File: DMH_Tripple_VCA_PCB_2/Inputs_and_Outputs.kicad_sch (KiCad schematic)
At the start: 0 parts

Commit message: Corrected header locations and placed pcb2 comps
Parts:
- added D6, D7, D8: LED_Dual_AKA, SynthStuff:LED_D3.0mm-2color, symbol Device:LED_Dual_AKA
- added J0: Conn_01x01, Connector_PinHeader_2.54mm:PinHeader_1x01_P2.54mm_Vertical, symbol Connector_Generic:Conn_01x01
- added J1, J10, J2, J3, J4, J5, J6, J7, J8, J9: TS_Jack_6.35mm_Sw, SynthStuff:CUI_MJ-63052A, symbol SynthStuff:TS_Jack_6.35mm_Sw
- added J200: IDC_02x05, SynthStuff:IDC-Header_2x05_P2.54mm_Vertical_BackBone, symbol SynthStuff:BackBone_Connector_10Pin
- added J50, J60, J70: Conn_01x06, Connector_PinHeader_2.54mm:PinHeader_1x06_P2.54mm_Vertical, symbol Connector_Generic:Conn_01x06
- added R53, R54, R55: 20k, Resistor_THT:R_Axial_DIN0207_L6.3mm_D2.5mm_P7.62mm_Horizontal, symbol Device:R_US
- added R56, R58, R60: 220R, Resistor_THT:R_Axial_DIN0207_L6.3mm_D2.5mm_P7.62mm_Horizontal, symbol Device:R_US
- added R57, R59, R61: 330R, Resistor_THT:R_Axial_DIN0207_L6.3mm_D2.5mm_P7.62mm_Horizontal, symbol Device:R_US
- added RV4, RV5, RV6: 100k, SynthStuff:Potentiometer_Alpha_RD901F-40-00D_Single_Vertical, symbol Device:R_Potentiometer_US
- added SW1, SW2, SW3: SW_DPDT, SynthStuff:Toggle_Switch_2_Poles_THT, symbol SynthStuff:Switch_DPDT
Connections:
- new net: J200.9 (Pin_9), J9.TN
- new net: J2.TN, J200.2 (Pin_2)
- new net: D6.1 (A1), R57.1
- new net: D6.3 (A2), R56.1
- new net: R57.2, SW1.4 (A)
- new net: R56.2, SW1.6 (C)
- new net: R61.2, SW3.4 (A)
- new net: R60.2, SW3.6 (C)
- new net: J1.TN, J200.1 (Pin_1)
- new net: J10.TN, J200.10 (Pin_10)
- new net: J200.3 (Pin_3), J3.TN
- new net: J200.4 (Pin_4), J4.TN
- new net: J200.5 (Pin_5), J5.TN
- new net: J200.6 (Pin_6), J6.TN
- new net: J200.7 (Pin_7), J7.TN
- new net: J200.8 (Pin_8), J8.TN
- new net: R54.1, RV5.1
- new net: R59.2, SW2.4 (A)
- new net: R58.2, SW2.6 (C)
- new net: D8.1 (A1), R61.1
- new net: D8.3 (A2), R60.1
- new net: R53.1, RV4.1
- new net: D7.3 (A2), R58.1
- new net: R55.1, RV6.1
- new net: D7.1 (A1), R59.1
- new net +12V: J50.1 (Pin_1), J60.1 (Pin_1), J70.1 (Pin_1), R53.2, R54.2, R55.2, SW1.5 (B), SW2.5 (B), SW3.5 (B)
- new net CV A Jack: J3.T
- new net CV B Jack: J6.T
- new net CV C Jack: J9.T
- new net GND: D6.2 (K), D7.2 (K), D8.2 (K), J0.1 (Pin_1), J1.S, J10.S, J2.S, J3.S, J4.S, J5.S, J50.5 (Pin_5), J50.6 (Pin_6), J6.S, J60.5 (Pin_5), J60.6 (Pin_6), J7.S, J70.5 (Pin_5), J70.6 (Pin_6), J8.S, J9.S, RV4.3, RV5.3, RV6.3
- new net Input A Jack: J1.T
- new net Input B Jack: J4.T
- new net Input C Jack: J7.T
- new net Mix Out Jack: J10.T
- new net Mute A Switch: J50.2 (Pin_2), SW1.1 (A)
- new net Mute B Switch: J60.2 (Pin_2), SW2.1 (A)
- new net Mute C Switch: J70.2 (Pin_2), SW3.1 (A)
- new net Offset A Pot: J50.4 (Pin_4), RV4.2
- new net Offset B Pot: J60.4 (Pin_4), RV5.2
- new net Offset C Pot: J70.4 (Pin_4), RV6.2
- new net Output A Jack: J2.T, J50.3 (Pin_3), SW1.2 (B)
- new net Output B Jack: J5.T, J60.3 (Pin_3), SW2.2 (B)
- new net Output C Jack: J70.3 (Pin_3), J8.T, SW3.2 (B)
- no-connect marks 0 -> 3
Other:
- note added: "PCB 2"

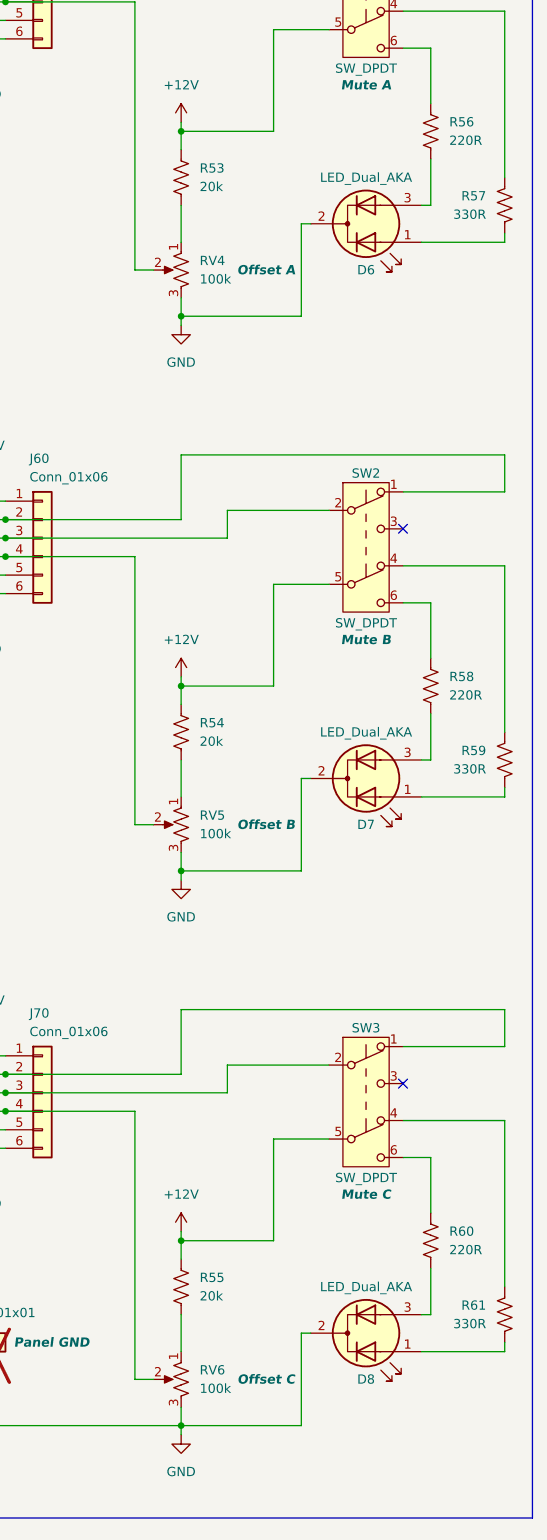
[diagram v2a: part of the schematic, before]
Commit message: Fixed mistakes in PCB 2
- Inverted offset potentiometers pinout
- LED resistors were too low, changed to 1k both colors
- Regenerated PCB 2 gerbers accordingly
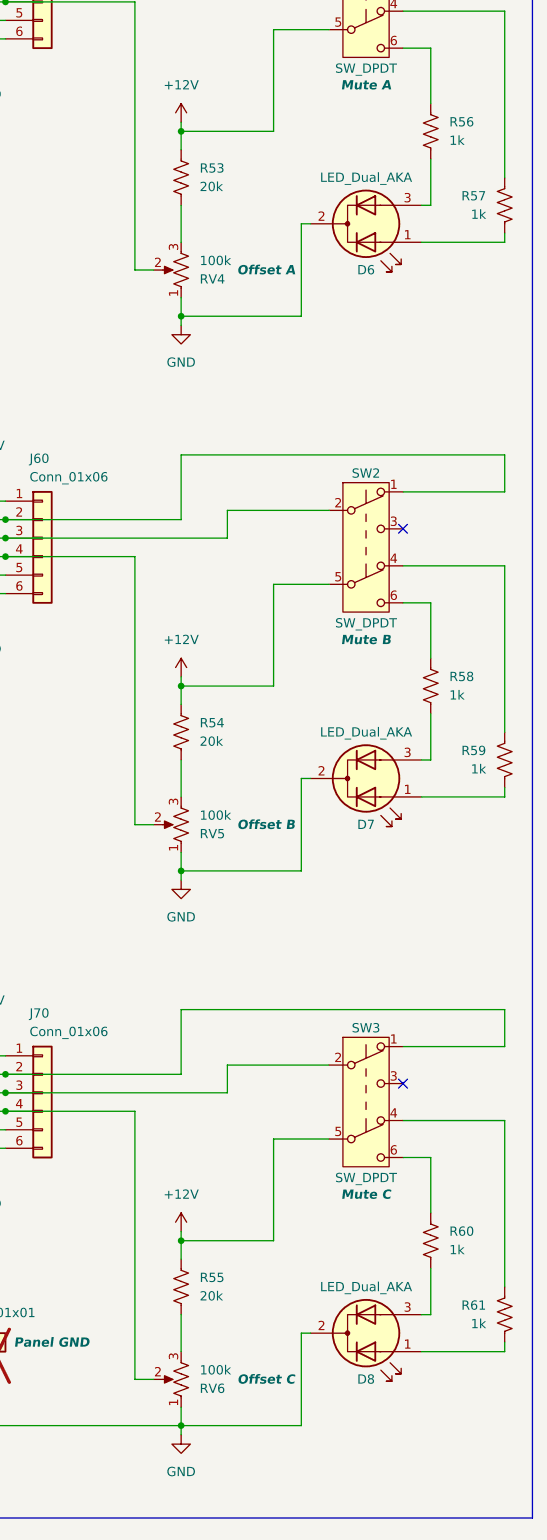
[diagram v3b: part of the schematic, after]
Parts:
- R56, R58, R60: value 220R -> 1k
- R57, R59, R61: value 330R -> 1k
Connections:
- net GND: now also RV4.1, RV5.1, RV6.1; no longer RV4.3, RV5.3, RV6.3
- net at R54.1: now also RV5.3; no longer RV5.1
- net at R53.1: now also RV4.3; no longer RV4.1
- net at R55.1: now also RV6.3; no longer RV6.1
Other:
- moved on the sheet: RV4, RV5, RV6
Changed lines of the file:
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@@
 			)
 		)
-		(property "Value" "220R"
+		(property "Value" "1k"
 			(at 182.88 58.4199 0)
 			(effects
@@
 				)
 				(hide yes)
+			)
+		)
+		(property "Function" ""
+			(at 180.34 57.15 0)
+			(effects
+				(font
+					(size 1.27 1.27)
+				)
 			)
 		)
@@
 	(symbol
 		(lib_id "Device:R_Potentiometer_US")
-		(at 146.05 152.4 0)
-		(mirror y)
+		(at 146.05 152.4 180)
 		(unit 1)
 		(exclude_from_sim no)
@@
 		(dnp no)
 		(property "Reference" "RV5"
-			(at 148.59 151.1299 0)
+			(at 148.59 153.6701 0)
 			(effects
 				(font
@@
 		)
 		(property "Value" "100k"
-			(at 148.59 153.6699 0)
+			(at 148.59 151.1301 0)
 			(effects
 				(font
@@
 			)
 		)
-		(property "Value" "220R"
+		(property "Value" "1k"
 			(at 182.88 210.8199 0)
 			(effects
@@
 				)
 				(hide yes)
+			)
+		)
+		(property "Function" ""
+			(at 180.34 209.55 0)
+			(effects
+				(font
+					(size 1.27 1.27)
+				)
 			)
 		)
@@
 	(symbol
 		(lib_id "Device:R_Potentiometer_US")
-		(at 146.05 76.2 0)
-		(mirror y)
+		(at 146.05 76.2 180)
 		(unit 1)
 		(exclude_from_sim no)
@@
 		(dnp no)
 		(property "Reference" "RV4"
-			(at 148.59 74.9299 0)
+			(at 148.59 77.4701 0)
 			(effects
 				(font
@@
 		)
 		(property "Value" "100k"
-			(at 148.59 77.4699 0)
+			(at 148.59 74.9301 0)
 			(effects
 				(font
@@
 			)
 		)
-		(property "Value" "220R"
+		(property "Value" "1k"
 			(at 182.88 134.6199 0)
 			(effects
@@
 				)
 				(hide yes)
+			)
+		)
+		(property "Function" ""
+			(at 180.34 133.35 0)
+			(effects
+				(font
+					(size 1.27 1.27)
+				)
 			)
 		)
@@
 			)
 		)
-		(property "Value" "330R"
+		(property "Value" "1k"
 			(at 187.96 220.9799 0)
 			(effects
@@
 	(symbol
 		(lib_id "Device:R_Potentiometer_US")
-		(at 146.05 228.6 0)
-		(mirror y)
+		(at 146.05 228.6 180)
 		(unit 1)
 		(exclude_from_sim no)
@@
 		(dnp no)
 		(property "Reference" "RV6"
-			(at 148.59 227.3299 0)
+			(at 148.59 229.8701 0)
 			(effects
 				(font
@@
 		)
 		(property "Value" "100k"
-			(at 148.59 229.8699 0)
+			(at 148.59 227.3301 0)
 			(effects
 				(font
@@
 			)
 		)
-		(property "Value" "330R"
+		(property "Value" "1k"
 			(at 187.96 68.5799 0)
 			(effects
@@
 				)
 				(hide yes)
+			)
+		)
+		(property "Function" ""
+			(at 190.5 67.31 0)
+			(effects
+				(font
+					(size 1.27 1.27)
+				)
 			)
 		)
@@
 			)
 		)
-		(property "Value" "330R"
+		(property "Value" "1k"
 			(at 187.96 144.7799 0)
 			(effects
@@
 			)
 		)
+		(property "Function" ""
+			(at 190.5 143.51 0)
+			(effects
+				(font
+					(size 1.27 1.27)
+				)
+			)
+		)
